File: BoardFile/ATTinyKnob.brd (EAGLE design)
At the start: 30.8 x 27.9 mm, 14 parts, among them U1 ATTINY_25_45_85

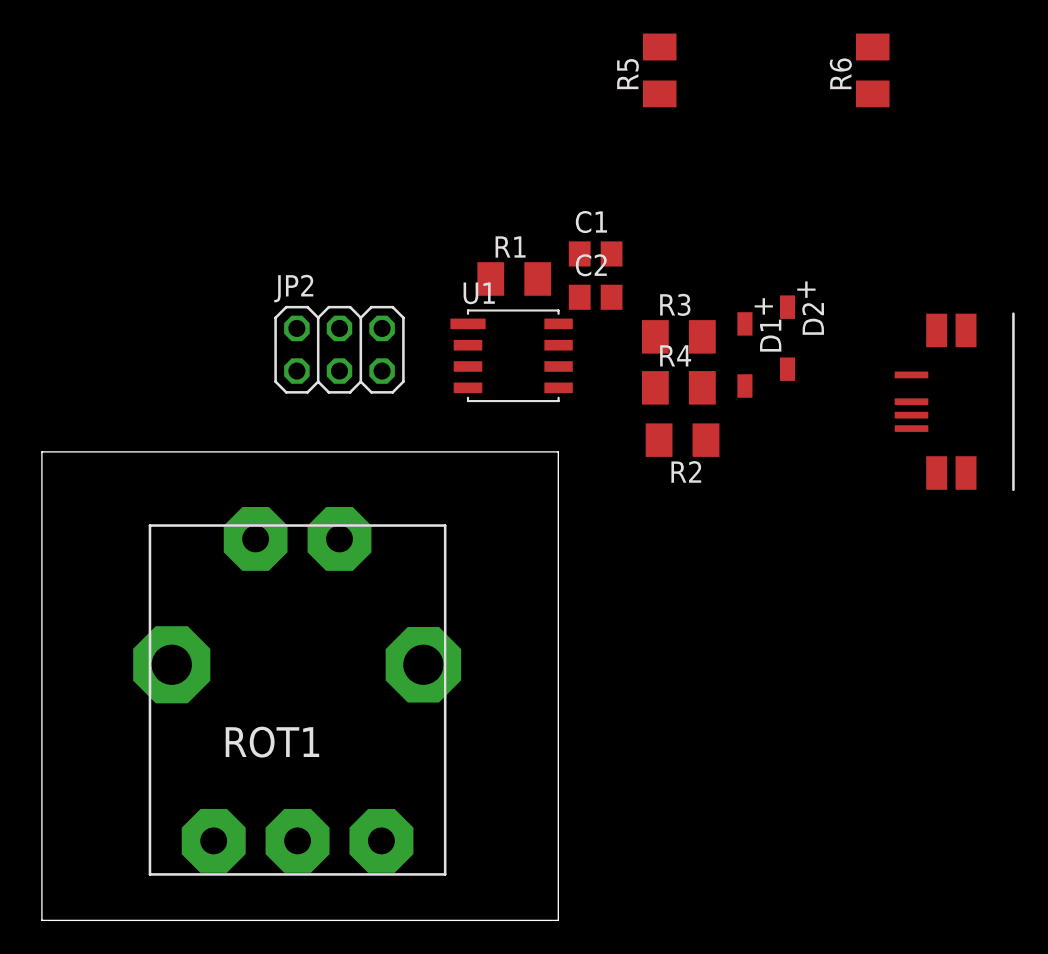
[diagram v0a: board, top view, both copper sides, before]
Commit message: Created board, added 3d files
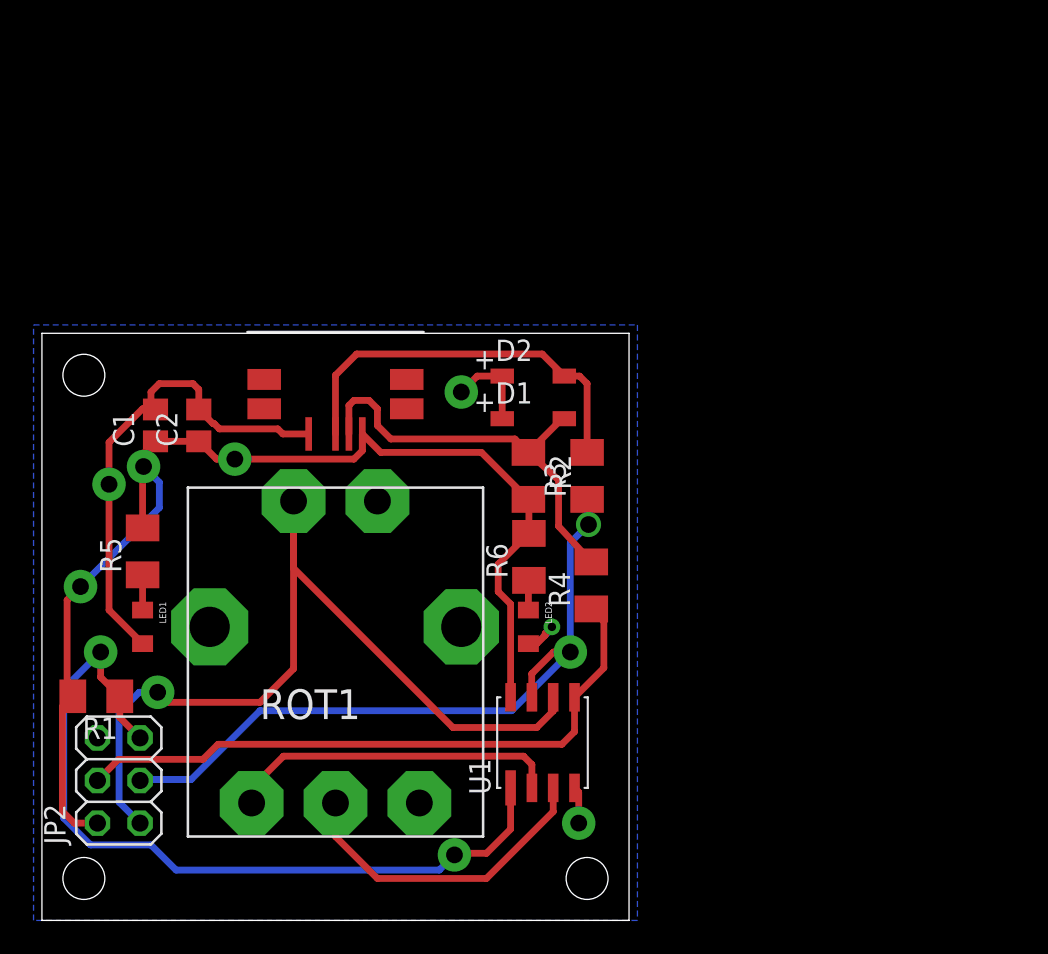
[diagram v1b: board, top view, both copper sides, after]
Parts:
- added LED1, LED2: LED_SMD_SM, DR:LED_SMD_SM
- moved R5 42.1 mm to (6.00, 22.0)
- moved R6 35.5 mm to (29.0, 21.7)
- moved R1 35.2 mm to (3.24, 13.4), turned to 180 degrees
- moved USB1 31.8 mm to (21.8, 30.5), turned to 180 degrees
- moved JP2 28.9 mm to (4.58, 8.34), turned to 90 degrees
- moved C1 28.2 mm to (6.77, 29.5), turned to 90 degrees
- moved U1 27.8 mm to (27.9, 7.90), turned to 90 degrees
- moved C2 24.9 mm to (9.35, 29.5), turned to 90 degrees
- moved D2 17.5 mm to (27.4, 32.5), turned to 0 degrees
- moved D1 15.5 mm to (27.4, 29.9), turned to 0 degrees
- moved R4 12.9 mm to (32.8, 20.0), turned to 90 degrees
- moved R3 9.93 mm to (32.5, 26.5), turned to 90 degrees
- moved R2 9.43 mm to (29.0, 26.5), turned to 270 degrees
- moved ROT1 3.20 mm to (17.5, 17.5)
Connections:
- removed net N$10: ROT1.S
- new net N$7: LED2.1, R6.1
- new net N$8: LED1.1, R5.1
- net +5V: now also R5.2, R6.2
- net GND: now also LED1.2, LED2.2
- net MISO: now also ROT1.S
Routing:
- net +5V: track 0.00 -> 69.9 mm, vias 0 -> 3
- net MISO: track 0.00 -> 53.7 mm, vias 0 -> 1
- net !RST: track 0.00 -> 48.3 mm, vias 0 -> 2
- net SCK: track 0.00 -> 43.0 mm, vias 0 -> 2
- net GND: track 0.00 -> 40.3 mm, vias 0 -> 4
- net MOSI: track 0.00 -> 38.0 mm
- net N$6: track 0.00 -> 25.4 mm
- net N$4: track 0.00 -> 23.9 mm
- net N$1: track 0.00 -> 20.0 mm
- net N$2: track 0.00 -> 19.1 mm
- net N$8: track 0.00 -> 2.10 mm
- net N$7: track 0.00 -> 1.78 mm
- added copper zone on layer 16, net GND
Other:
- board size 30.8 x 27.9 mm -> 35 x 35 mm

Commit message: Added through hole usb
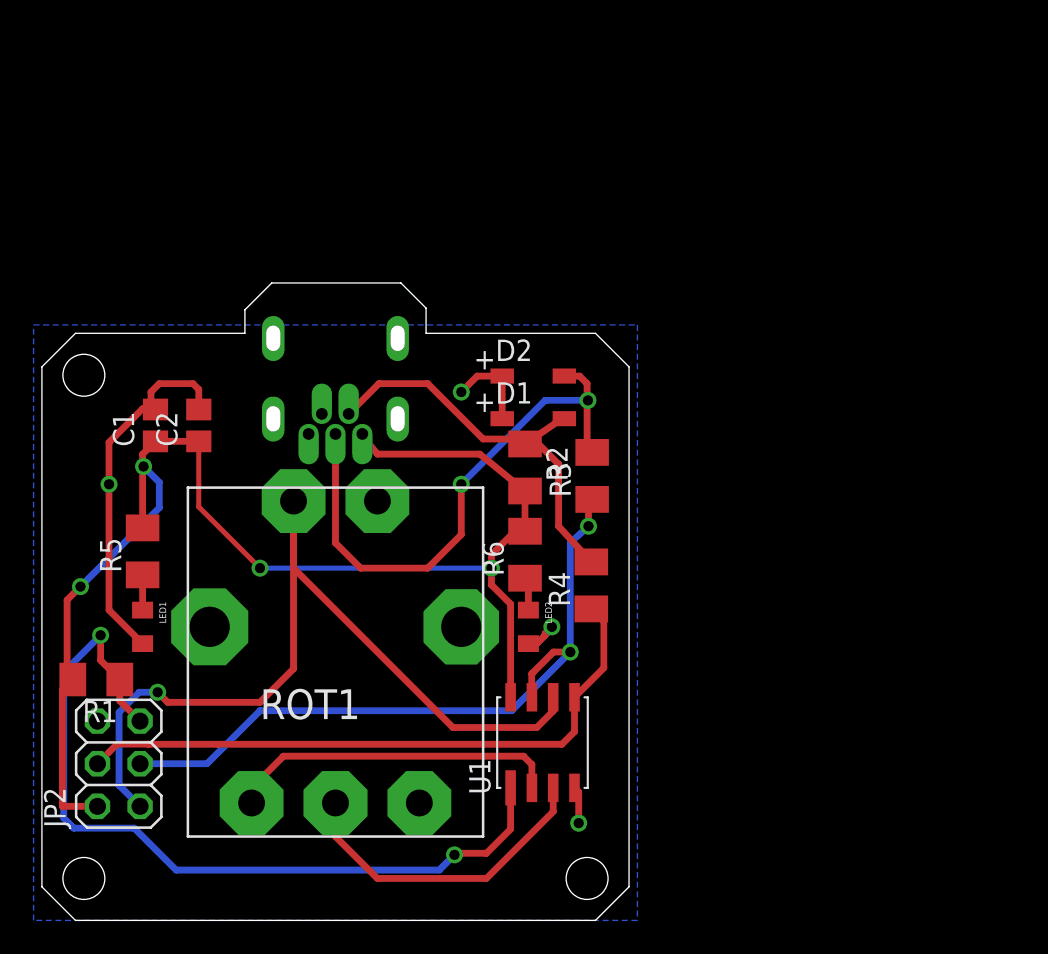
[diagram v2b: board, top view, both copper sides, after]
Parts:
- USB1: value USB_MINI -> USB_MINIUSB_MINI_TH_RIGHTANG; device DR:USB_MINI -> DR:USB_MINI_TH_RIGHTANGLE
- moved USB1 6.04 mm to (15.9, 29.0), turned to 0 degrees
- moved JP2 1.00 mm to (4.58, 9.34)
- moved R1 1.00 mm to (3.24, 14.4)
- moved R2 0.54 mm to (28.8, 27.0)
- moved R3 0.30 mm to (32.8, 26.5)
- moved R6 0.26 mm to (28.8, 21.8)
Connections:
- net GND: now also USB1.6, USB1.7, USB1.8, USB1.9
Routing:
- net +5V: track 69.9 -> 81.5 mm, vias 3 -> 4
- net N$4: track 23.9 -> 33.9 mm, vias 0 -> 2
- net GND: track 40.3 -> 33.1 mm
- net MISO: track 53.7 -> 52.7 mm
- net !RST: track 48.3 -> 49.3 mm
- net N$6: track 25.4 -> 24.6 mm
- net SCK: track 43.0 -> 42.4 mm
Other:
- board size 35 x 35 mm -> 35 x 38 mm

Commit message: Board built
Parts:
- moved D1 0.80 mm to (27.4, 30.7)
- moved D2 0.60 mm to (27.4, 33.0)
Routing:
- net GND: track 33.1 -> 41.6 mm
- net +5V: track 81.5 -> 83.0 mm
- net N$6: track 24.6 -> 25.2 mm
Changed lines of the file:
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@@
 <attribute name="VALUE" x="31.34" y="20.53" size="1.27" layer="27" rot="R90"/>
 </element>
-<element name="D1" library="DR" package="SOD123" value="DIODESOD123" x="27.44" y="29.91" smashed="yes">
-<attribute name="NAME" x="27.04" y="30.81" size="1.27" layer="25"/>
-</element>
-<element name="D2" library="DR" package="SOD123" value="DIODESOD123" x="27.44" y="32.45" smashed="yes">
-<attribute name="NAME" x="27.04" y="33.35" size="1.27" layer="25"/>
+<element name="D1" library="DR" package="SOD123" value="DIODESOD123" x="27.44" y="30.71" smashed="yes">
+<attribute name="NAME" x="27.04" y="31.61" size="1.27" layer="25"/>
+</element>
+<element name="D2" library="DR" package="SOD123" value="DIODESOD123" x="27.44" y="33.05" smashed="yes">
+<attribute name="NAME" x="27.04" y="33.95" size="1.27" layer="25"/>
 </element>
 <element name="C1" library="DR" package="C0805" value="100n" x="6.77" y="29.51" smashed="yes" rot="R90">
@@
 <wire x1="6.73" y1="30.5" x2="6.77" y2="30.46" width="0.4064" layer="1"/>
 <via x="25" y="31.5" extent="1-16" drill="0.6096"/>
-<wire x1="25" y1="31.5" x2="25.95" y2="32.45" width="0.4064" layer="1"/>
-<wire x1="25.95" y1="32.45" x2="27.44" y2="32.45" width="0.4064" layer="1"/>
-<wire x1="27.44" y1="29.91" x2="27.44" y2="32.45" width="0.4064" layer="1"/>
+<wire x1="25" y1="31.5" x2="26.55" y2="33.05" width="0.4064" layer="1"/>
+<wire x1="26.55" y1="33.05" x2="27.44" y2="33.05" width="0.4064" layer="1"/>
+<wire x1="27.44" y1="30.71" x2="27.44" y2="33.05" width="0.4064" layer="1"/>
 <wire x1="31.75" y1="7.9" x2="32" y2="7.65" width="0.4064" layer="1"/>
 <wire x1="32" y1="7.65" x2="32" y2="5.8" width="0.4064" layer="1"/>
@@
 <contactref element="USB1" pad="8"/>
 <contactref element="USB1" pad="6"/>
+<wire x1="15.9" y1="29" x2="14.5" y2="27.6" width="0.3048" layer="1"/>
+<wire x1="14.5" y1="27.6" x2="12" y2="27.6" width="0.3048" layer="1"/>
+<wire x1="12" y1="27.6" x2="10.4556" y2="29.1444" width="0.3048" layer="1"/>
+<wire x1="10.4556" y1="29.1444" x2="10.4556" y2="29.35729375" width="0.3048" layer="1"/>
+<wire x1="10.4556" y1="29.35729375" x2="10.24729375" y2="29.5656" width="0.3048" layer="1"/>
+<wire x1="10.24729375" y1="29.5656" x2="10.2444" y2="29.5656" width="0.3048" layer="1"/>
+<wire x1="10.2444" y1="29.5656" x2="9.35" y2="30.46" width="0.3048" layer="1"/>
+<wire x1="21.2086" y1="29.889" x2="21.2086" y2="34.6896" width="0" layer="19" extent="1-1"/>
+<wire x1="25" y1="31.5" x2="21.2086" y2="29.889" width="0" layer="19" extent="1-1"/>
+<wire x1="13.7918" y1="29.889" x2="15.9" y2="29" width="0" layer="19" extent="1-1"/>
+<wire x1="13.7918" y1="34.6896" x2="13.7918" y2="29.889" width="0" layer="19" extent="1-1"/>
 </signal>
 <signal name="N$1">
@@
 <contactref element="C1" pad="1"/>
 <contactref element="JP2" pad="2"/>
-<contactref element="R1" pad="2"/>
-<contactref element="R2" pad="2"/>
 <contactref element="R5" pad="2"/>
 <contactref element="R6" pad="2"/>
@@
 <wire x1="6" y1="27.79" x2="6.77" y2="28.56" width="0.4064" layer="1"/>
 <wire x1="6.77" y1="28.56" x2="9.35" y2="28.56" width="0.4064" layer="1"/>
-<wire x1="28.8" y1="25.6" x2="26.1" y2="27.8" width="0.4064" layer="1"/>
 <wire x1="27.94" y1="13.3" x2="27.94" y2="18.86" width="0.4064" layer="1"/>
 <wire x1="27.94" y1="18.86" x2="26.8" y2="20" width="0.4064" layer="1"/>
@@
 <wire x1="6.0579" y1="27.0579" x2="6" y2="27" width="0.4064" layer="1"/>
 <wire x1="7" y1="24.6" x2="7" y2="26.1158" width="0.4064" layer="16"/>
-<wire x1="1.5" y1="14.7" x2="1.84" y2="14.36" width="0.4064" layer="1"/>
 <wire x1="1.5" y1="14.7" x2="1.5" y2="19.1" width="0.4064" layer="1"/>
-<wire x1="1.84" y1="14.36" x2="1.2192" y2="13.7392" width="0.4064" layer="1"/>
-<wire x1="1.2192" y1="13.7392" x2="1.2192" y2="6.8" width="0.4064" layer="1"/>
+<wire x1="1.2192" y1="13.7392" x2="1.2192" y2="13" width="0.4064" layer="1"/>
+<wire x1="1.2192" y1="13" x2="1.2192" y2="6.8" width="0.4064" layer="1"/>
 <wire x1="1.2192" y1="6.8" x2="3.31" y2="6.8" width="0.4064" layer="1"/>
 <wire x1="1.5" y1="19.1" x2="2.3" y2="19.9" width="0.4064" layer="1"/>
-<contactref element="USB1" pad="1"/>
-<wire x1="26.1" y1="27.8" x2="20" y2="27.8" width="0.4064" layer="1"/>
-<wire x1="20" y1="27.8" x2="19.1004" y2="28.8996" width="0.4064" layer="1"/>
-<wire x1="19.1004" y1="28.8996" x2="19.1004" y2="29" width="0.254" layer="1"/>
 <wire x1="9.35" y1="28.56" x2="9.35" y2="24.65" width="0.3048" layer="1"/>
 <wire x1="9.35" y1="24.65" x2="13" y2="21" width="0.3048" layer="1"/>
@@
 <wire x1="28.2" y1="23.2" x2="28.8" y2="23.2" width="0.4064" layer="1"/>
 <wire x1="26.8" y1="21.8" x2="28.2" y2="23.2" width="0.4064" layer="1"/>
-<wire x1="28.8" y1="25.6" x2="28.8" y2="23.2" width="0.4064" layer="1"/>
+<contactref element="USB1" pad="1"/>
+<contactref element="R2" pad="2"/>
+<contactref element="R1" pad="2"/>
+<wire x1="21.85564375" y1="27.9459" x2="21.90974375" y2="28" width="0.254" layer="1"/>
+<wire x1="19.1004" y1="29" x2="20.1545" y2="27.9459" width="0.254" layer="1"/>
+<wire x1="20.1545" y1="27.9459" x2="21.85564375" y2="27.9459" width="0.254" layer="1"/>
+<wire x1="28.4" y1="25.6" x2="28.8" y2="25.6" width="0.254" layer="1"/>
+<wire x1="21.90974375" y1="28" x2="26" y2="28" width="0.254" layer="1"/>
+<wire x1="26" y1="28" x2="28.4" y2="25.6" width="0.254" layer="1"/>
+<wire x1="1.6" y1="14.6" x2="1.5" y2="14.7" width="0.254" layer="1"/>
+<wire x1="1.84" y1="14.36" x2="1.84" y2="14.84" width="0.254" layer="1"/>
+<wire x1="1.84" y1="14.84" x2="2" y2="15" width="0.254" layer="1"/>
+<wire x1="1.84" y1="14.84" x2="1.6" y2="14.6" width="0.254" layer="1"/>
+<wire x1="1.84" y1="14.36" x2="1.84" y2="13.6208" width="0.254" layer="1"/>
+<wire x1="1.84" y1="13.6208" x2="1.2192" y2="13" width="0.254" layer="1"/>
+<wire x1="28.8" y1="25.6" x2="28.8" y2="23.2" width="0.254" layer="1"/>
 </signal>
 <signal name="SCK">
@@
 <contactref element="R3" pad="2"/>
 <contactref element="D2" pad="2"/>
-<wire x1="31.14" y1="32.45" x2="32.05" y2="32.45" width="0.4064" layer="1"/>
-<wire x1="32.05" y1="32.45" x2="32.5" y2="32" width="0.4064" layer="1"/>
+<wire x1="31.14" y1="33.05" x2="31.45" y2="33.05" width="0.4064" layer="1"/>
+<wire x1="31.45" y1="33.05" x2="32.5" y2="32" width="0.4064" layer="1"/>
 <wire x1="32.5" y1="32" x2="32.5" y2="31" width="0.4064" layer="1"/>
 <wire x1="32.5" y1="31" x2="32.5" y2="28.16" width="0.4064" layer="1"/>
@@
 <contactref element="D1" pad="2"/>
 <contactref element="R2" pad="1"/>
-<wire x1="28.8" y1="28.4" x2="31.01" y2="29.91" width="0.4064" layer="1"/>
-<wire x1="31.01" y1="29.91" x2="31.14" y2="29.91" width="0.4064" layer="1"/>
+<wire x1="28.8" y1="28.4" x2="30.761684375" y2="29.740334375" width="0.4064" layer="1"/>
+<wire x1="30.761684375" y1="29.740334375" x2="31.14" y2="30.71" width="0.4064" layer="1"/>
 <wire x1="30.8" y1="23.5" x2="32.75" y2="21.37" width="0.4064" layer="1"/>
-<wire x1="30.8" y1="26.4" x2="30.8" y2="26" width="0.4064" layer="1"/>
-<wire x1="30.8" y1="26" x2="30.8" y2="23.5" width="0.4064" layer="1"/>
+<wire x1="30.8" y1="27.2" x2="30.8" y2="23.5" width="0.4064" layer="1"/>
 <wire x1="28.2" y1="28.7" x2="28.8" y2="28.4" width="0.4064" layer="1"/>
 <contactref element="USB1" pad="2"/>
@@
 <wire x1="20.0938" y1="32" x2="23" y2="32" width="0.4064" layer="1"/>
 <wire x1="23" y1="32" x2="26.3" y2="28.7" width="0.4064" layer="1"/>
-<wire x1="30.8" y1="26.4" x2="30.8" y2="27.2" width="0.4064" layer="1"/>
 <wire x1="29.6" y1="28.4" x2="28.8" y2="28.4" width="0.4064" layer="1"/>
 <wire x1="30.8" y1="27.2" x2="29.6" y2="28.4" width="0.4064" layer="1"/>
-</signal>
-<signal name="N$3">
 </signal>
 <signal name="N$7">
@@
 <wire x1="6" y1="18.5" x2="6" y2="20.6" width="0.4064" layer="1"/>
 </signal>
+<signal name="N$5">
+</signal>
 </signals>
